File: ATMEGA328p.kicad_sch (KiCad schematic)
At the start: 10 parts, among them SW1 SW_Push, SW2 SW_Push, SW3 SW_Wuerth_450301014042, U2 ATmega328-P, U3 DS3231M

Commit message: value addition & led arrangement
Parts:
- R2, R3, R4, R5: value R_US -> 1k; footprint Resistor_THT:R_Axial_DIN0204_L3.6mm_D1.6mm_P7.62mm_Horizontal -> Resistor_THT:R_Axial_DIN0207_L6.3mm_D2.5mm_P10.16mm_Horizontal
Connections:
- net RST: now reaches U2.1 (~{RESET}/PC6)
- net RST: now also U3.4 (~{RST})
- net Led D: now reaches U2.11 (PD5)
- net Led E: now reaches U2.12 (PD6)
- net Led F: now reaches U2.13 (PD7)
- net Led G: now reaches U2.14 (PB0)
- net Led A: now reaches U2.4 (PD2)
- net Led B: now reaches U2.5 (PD3)
- net Led C: now reaches U2.6 (PD4)
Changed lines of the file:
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@@
+	(wire
+		(pts
+			(xy 81.28 39.37) (xy 95.25 39.37)
+		)
+		(stroke
+			(width 0)
+			(type default)
+		)
+	)
 	(wire
 		(pts
@@
 	(wire
 		(pts
+			(xy 81.28 97.79) (xy 90.17 97.79)
+		)
+		(stroke
+			(width 0)
+			(type default)
+		)
+	)
+	(wire
+		(pts
 			(xy 231.14 58.42) (xy 237.49 58.42)
 		)
@@
 	(wire
 		(pts
+			(xy 81.28 77.47) (xy 88.9 77.47)
+		)
+		(stroke
+			(width 0)
+			(type default)
+		)
+	)
+	(wire
+		(pts
 			(xy 144.78 57.15) (xy 144.78 62.23)
 		)
@@
 	(wire
 		(pts
+			(xy 81.28 90.17) (xy 90.17 90.17)
+		)
+		(stroke
+			(width 0)
+			(type default)
+		)
+	)
+	(wire
+		(pts
 			(xy 81.28 69.85) (xy 95.25 69.85)
 		)
@@
 	(wire
 		(pts
+			(xy 81.28 95.25) (xy 90.17 95.25)
+		)
+		(stroke
+			(width 0)
+			(type default)
+		)
+	)
+	(wire
+		(pts
 			(xy 66.04 107.95) (xy 96.52 107.95)
 		)
@@
 	(wire
 		(pts
+			(xy 81.28 100.33) (xy 90.17 100.33)
+		)
+		(stroke
+			(width 0)
+			(type default)
+		)
+	)
+	(wire
+		(pts
 			(xy 81.28 74.93) (xy 90.17 74.93)
 		)
@@
 	(wire
 		(pts
+			(xy 81.28 87.63) (xy 90.17 87.63)
+		)
+		(stroke
+			(width 0)
+			(type default)
+		)
+	)
+	(wire
+		(pts
 			(xy 173.99 74.93) (xy 185.42 74.93)
 		)
@@
 		(pts
 			(xy 81.28 64.77) (xy 90.17 64.77)
+		)
+		(stroke
+			(width 0)
+			(type default)
+		)
+	)
+	(wire
+		(pts
+			(xy 81.28 92.71) (xy 90.17 92.71)
 		)
 		(stroke
@@
 		)
 	)
+	(label "Led A"
+		(at 82.55 87.63 0)
+		(fields_autoplaced yes)
+		(effects
+			(font
+				(size 1.27 1.27)
+			)
+			(justify left bottom)
+		)
+	)
+	(label "RST"
+		(at 176.53 82.55 0)
+		(fields_autoplaced yes)
+		(effects
+			(font
+				(size 1.27 1.27)
+			)
+			(justify left bottom)
+		)
+	)
+	(label "Led F"
+		(at 82.55 100.33 0)
+		(fields_autoplaced yes)
+		(effects
+			(font
+				(size 1.27 1.27)
+			)
+			(justify left bottom)
+		)
+	)
+	(label "RST"
+		(at 86.36 77.47 0)
+		(fields_autoplaced yes)
+		(effects
+			(font
+				(size 1.27 1.27)
+			)
+			(justify left bottom)
+		)
+	)
 	(label "SDA"
 		(at 83.82 72.39 0)
@@
 		)
 	)
+	(label "Led E"
+		(at 82.55 97.79 0)
+		(fields_autoplaced yes)
+		(effects
+			(font
+				(size 1.27 1.27)
+			)
+			(justify left bottom)
+		)
+	)
+	(label "Led F"
+		(at 82.55 100.33 0)
+		(fields_autoplaced yes)
+		(effects
+			(font
+				(size 1.27 1.27)
+			)
+			(justify left bottom)
+		)
+	)
 	(label "hour"
 		(at 82.55 67.31 0)
@@
 		)
 	)
+	(label "Led D"
+		(at 82.55 95.25 0)
+		(fields_autoplaced yes)
+		(effects
+			(font
+				(size 1.27 1.27)
+			)
+			(justify left bottom)
+		)
+	)
 	(label "Selector"
 		(at 82.55 64.77 0)
@@
 		)
 	)
+	(label "Led C"
+		(at 82.55 92.71 0)
+		(fields_autoplaced yes)
+		(effects
+			(font
+				(size 1.27 1.27)
+			)
+			(justify left bottom)
+		)
+	)
+	(label "Led B"
+		(at 82.55 90.17 0)
+		(fields_autoplaced yes)
+		(effects
+			(font
+				(size 1.27 1.27)
+			)
+			(justify left bottom)
+		)
+	)
 	(label "SCL"
 		(at 83.82 74.93 0)
+		(fields_autoplaced yes)
+		(effects
+			(font
+				(size 1.27 1.27)
+			)
+			(justify left bottom)
+		)
+	)
+	(label "Led G"
+		(at 85.09 39.37 0)
 		(fields_autoplaced yes)
 		(effects
@@
 			)
 		)
-		(property "Value" "R_US"
+		(property "Value" "1k"
 			(at 174.752 70.358 0)
 			(effects
@@
 			)
 		)
-		(property "Footprint" "Resistor_THT:R_Axial_DIN0204_L3.6mm_D1.6mm_P7.62mm_Horizontal"
+		(property "Footprint" "Resistor_THT:R_Axial_DIN0207_L6.3mm_D2.5mm_P10.16mm_Horizontal"
 			(at 175.006 68.834 90)
 			(effects
@@
 			)
 		)
-		(property "Value" "R_US"
+		(property "Value" "1k"
 			(at 220.98 76.1999 0)
 			(effects
@@
 			)
 		)
-		(property "Footprint" "Resistor_THT:R_Axial_DIN0204_L3.6mm_D1.6mm_P7.62mm_Horizontal"
+		(property "Footprint" "Resistor_THT:R_Axial_DIN0207_L6.3mm_D2.5mm_P10.16mm_Horizontal"
 			(at 219.456 75.184 90)
 			(effects
@@
 			)
 		)
-		(property "Value" "R_US"
+		(property "Value" "1k"
 			(at 182.88 69.8499 0)
 			(effects
@@
 			)
 		)
-		(property "Footprint" "Resistor_THT:R_Axial_DIN0204_L3.6mm_D1.6mm_P7.62mm_Horizontal"
+		(property "Footprint" "Resistor_THT:R_Axial_DIN0207_L6.3mm_D2.5mm_P10.16mm_Horizontal"
 			(at 181.356 68.834 90)
 			(effects
@@
 			)
 		)
-		(property "Value" "R_US"
+		(property "Value" "1k"
 			(at 214.376 69.85 0)
 			(effects
@@
 			)
 		)
-		(property "Footprint" "Resistor_THT:R_Axial_DIN0204_L3.6mm_D1.6mm_P7.62mm_Horizontal"
+		(property "Footprint" "Resistor_THT:R_Axial_DIN0207_L6.3mm_D2.5mm_P10.16mm_Horizontal"
 			(at 214.376 68.834 90)
 			(effects

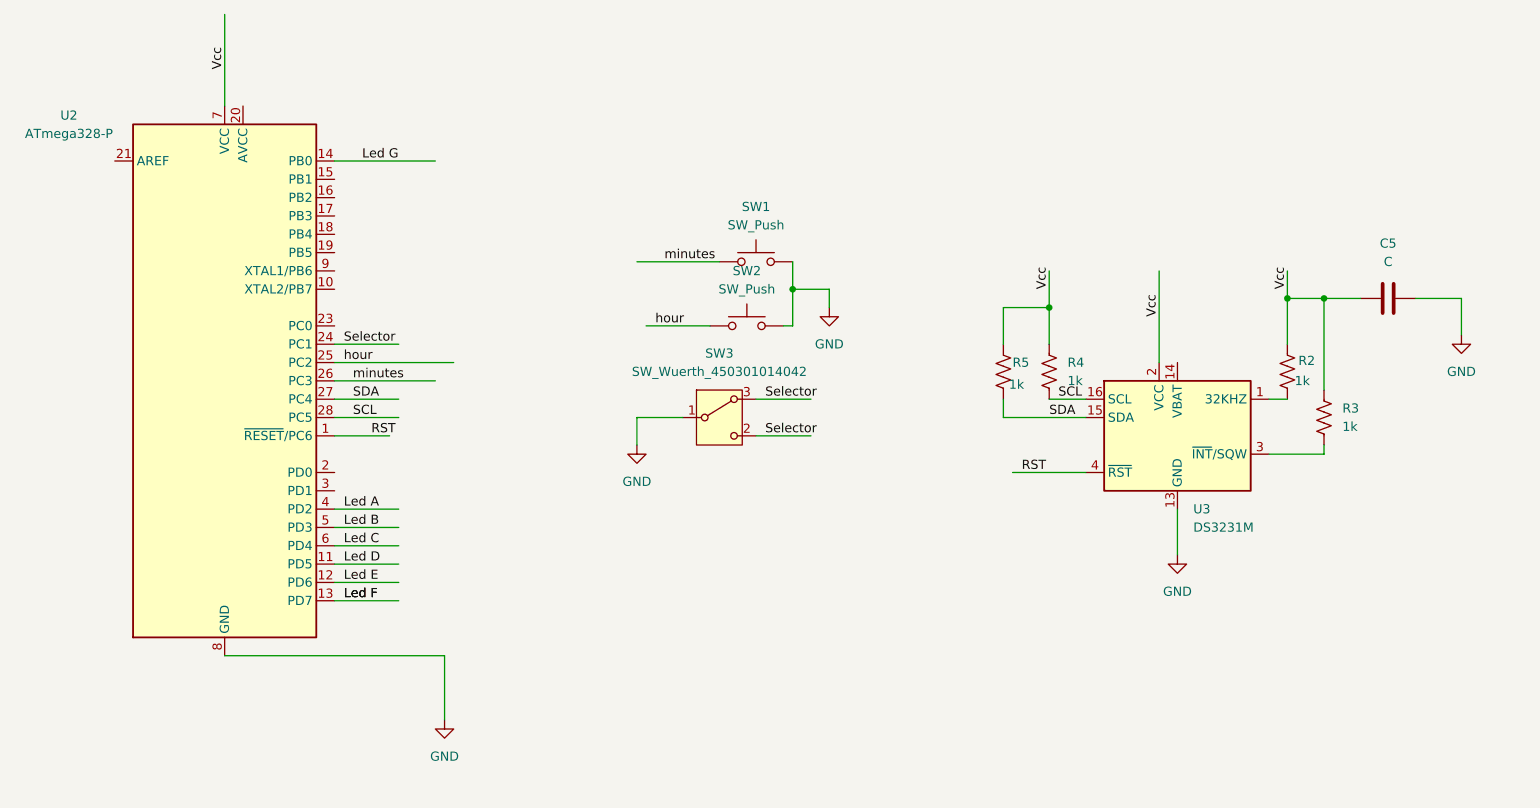
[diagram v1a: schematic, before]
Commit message: display board
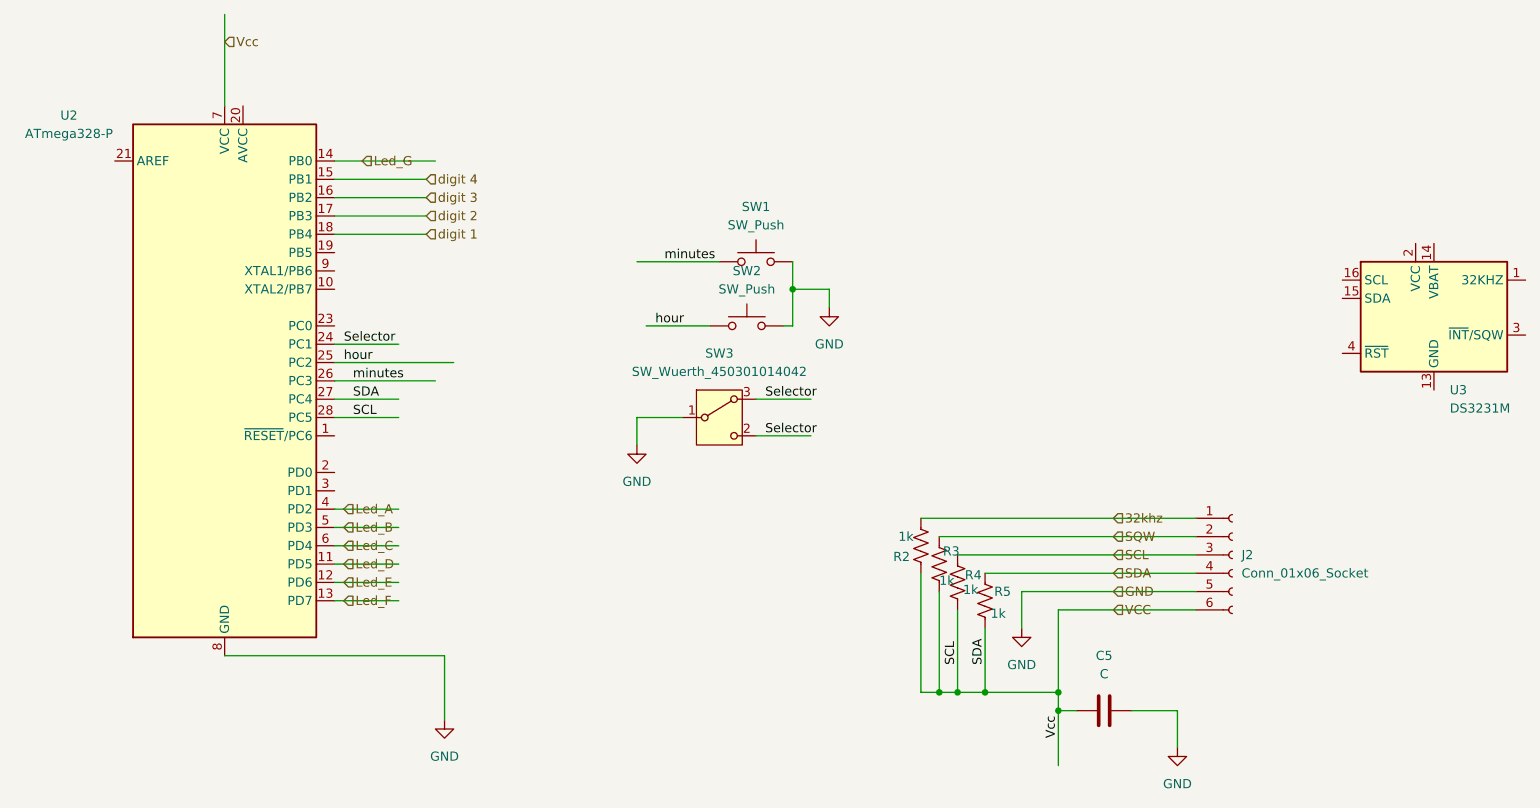
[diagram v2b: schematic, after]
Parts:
- added J2: Conn_01x06_Socket, Connector_PinHeader_2.54mm:PinHeader_1x06_P2.54mm_Vertical, symbol Connector:Conn_01x06_Socket
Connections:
- net GND: now also J2.5 (Pin_5); no longer U3.10 (GND), U3.11 (GND), U3.12 (GND), U3.13 (GND), U3.5 (GND), U3.6 (GND), U3.7 (GND), U3.8 (GND), U3.9 (GND)
- net SCL: now also C5.1, R2.1, R3.2, R4.1, R5.1, R5.2, U2.27 (PC4), U2.7 (VCC), J2.3 (Pin_3), J2.4 (Pin_4), J2.6 (Pin_6); no longer U3.16 (SCL)
- net digit 4: now reaches U2.15 (PB1)
- net digit 3: now reaches U2.16 (PB2)
- net digit 2: now reaches U2.17 (PB3)
- net digit 1: now reaches U2.18 (PB4)
- net at U3.3 (~{INT}/SQW): no longer R3.2
- net at U3.1 (32KHZ): no longer R2.2
- net Led A renamed Led_A
- net Led B renamed Led_B
- net Led C renamed Led_C
- net Led D renamed Led_D
- net Led E renamed Led_E
- net Led F renamed Led_F
- net Led G renamed Led_G
- net RST: no longer names the net of U2.1 (~{RESET}/PC6)
- net RST: no longer U3.4 (~{RST})
- removed net SDA: R5.2, U2.27 (PC4), U3.15 (SDA)
- removed net Vcc: C5.1, R2.1, R3.1, R4.1, R5.1, U2.7 (VCC), U3.2 (VCC)
- new net: U3.10 (GND), U3.11 (GND), U3.12 (GND), U3.13 (GND), U3.5 (GND), U3.6 (GND), U3.7 (GND), U3.8 (GND), U3.9 (GND)
- new net 32khz: J2.1 (Pin_1), R2.2
- new net SQW: J2.2 (Pin_2), R3.1
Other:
- moved on the sheet: C5, R2, R3, R4, R5, U3

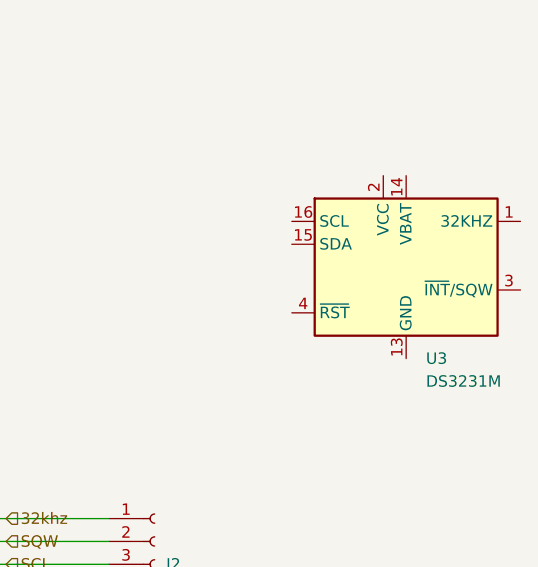
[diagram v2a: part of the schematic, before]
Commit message: Vcc plane
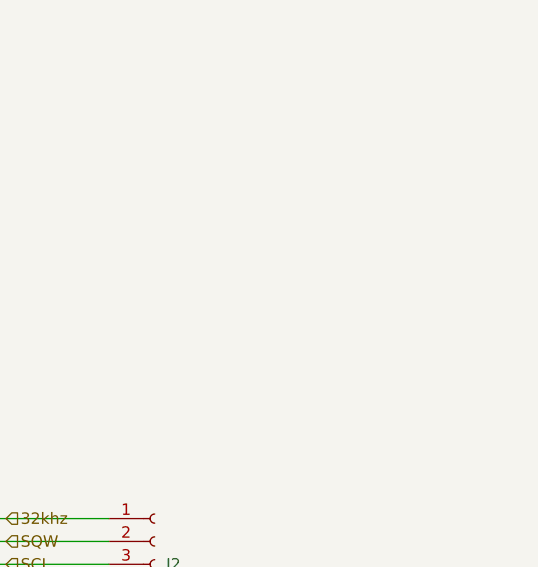
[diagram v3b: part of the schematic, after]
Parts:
- removed U3: DS3231M, Package_SO:SOIC-16W_7.5x10.3mm_P1.27mm, symbol Timer_RTC:DS3231M
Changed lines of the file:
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@@
-	)
-	(symbol
-		(lib_id "Timer_RTC:DS3231M")
-		(at 233.68 60.96 0)
-		(unit 1)
-		(exclude_from_sim no)
-		(in_bom yes)
-		(on_board yes)
-		(dnp no)
-		(fields_autoplaced yes)
-		(property "Reference" "U3"
-			(at 235.8741 71.12 0)
-			(effects
-				(font
-					(size 1.27 1.27)
-				)
-				(justify left)
-			)
-		)
-		(property "Value" "DS3231M"
-			(at 235.8741 73.66 0)
-			(effects
-				(font
-					(size 1.27 1.27)
-				)
-				(justify left)
-			)
-		)
-		(property "Footprint" "Package_SO:SOIC-16W_7.5x10.3mm_P1.27mm"
-			(at 233.68 76.2 0)
-			(effects
-				(font
-					(size 1.27 1.27)
-				)
-				(hide yes)
-			)
-		)
-		(property "Datasheet" "http://datasheets.maximintegrated.com/en/ds/DS3231.pdf"
-			(at 240.538 59.69 0)
-			(effects
-				(font
-					(size 1.27 1.27)
-				)
-				(hide yes)
-			)
-		)
-		(property "Description" "Extremely Accurate I2C-Integrated RTC/TCXO/Crystal SOIC-16"
-			(at 233.68 60.96 0)
-			(effects
-				(font
-					(size 1.27 1.27)
-				)
-				(hide yes)
-			)
-		)
-		(pin "4"
-		)
-		(pin "16"
-		)
-		(pin "10"
-		)
-		(pin "3"
-		)
-		(pin "1"
-		)
-		(pin "7"
-		)
-		(pin "15"
-		)
-		(pin "11"
-		)
-		(pin "9"
-		)
-		(pin "8"
-		)
-		(pin "13"
-		)
-		(pin "12"
-		)
-		(pin "14"
-		)
-		(pin "6"
-		)
-		(pin "2"
-		)
-		(pin "5"
-		)
-		(instances
-			(project ""
-				(path "/069826f8-6630-4c5a-baa3-a392b66f0264/2cdec6e4-2654-4a7b-b8ea-f82745c18c61"
-					(reference "U3")
-					(unit 1)
-				)
-			)
-		)
 	)
 	(symbol
